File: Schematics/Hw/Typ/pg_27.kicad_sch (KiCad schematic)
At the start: 29 parts, among them U2901 F04, U2902 F04, U2903 F02, U2904 F02, U2905 F02, U2906 F02, U2907 F10, U2908 F138, U2909 F00, U2910 F10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

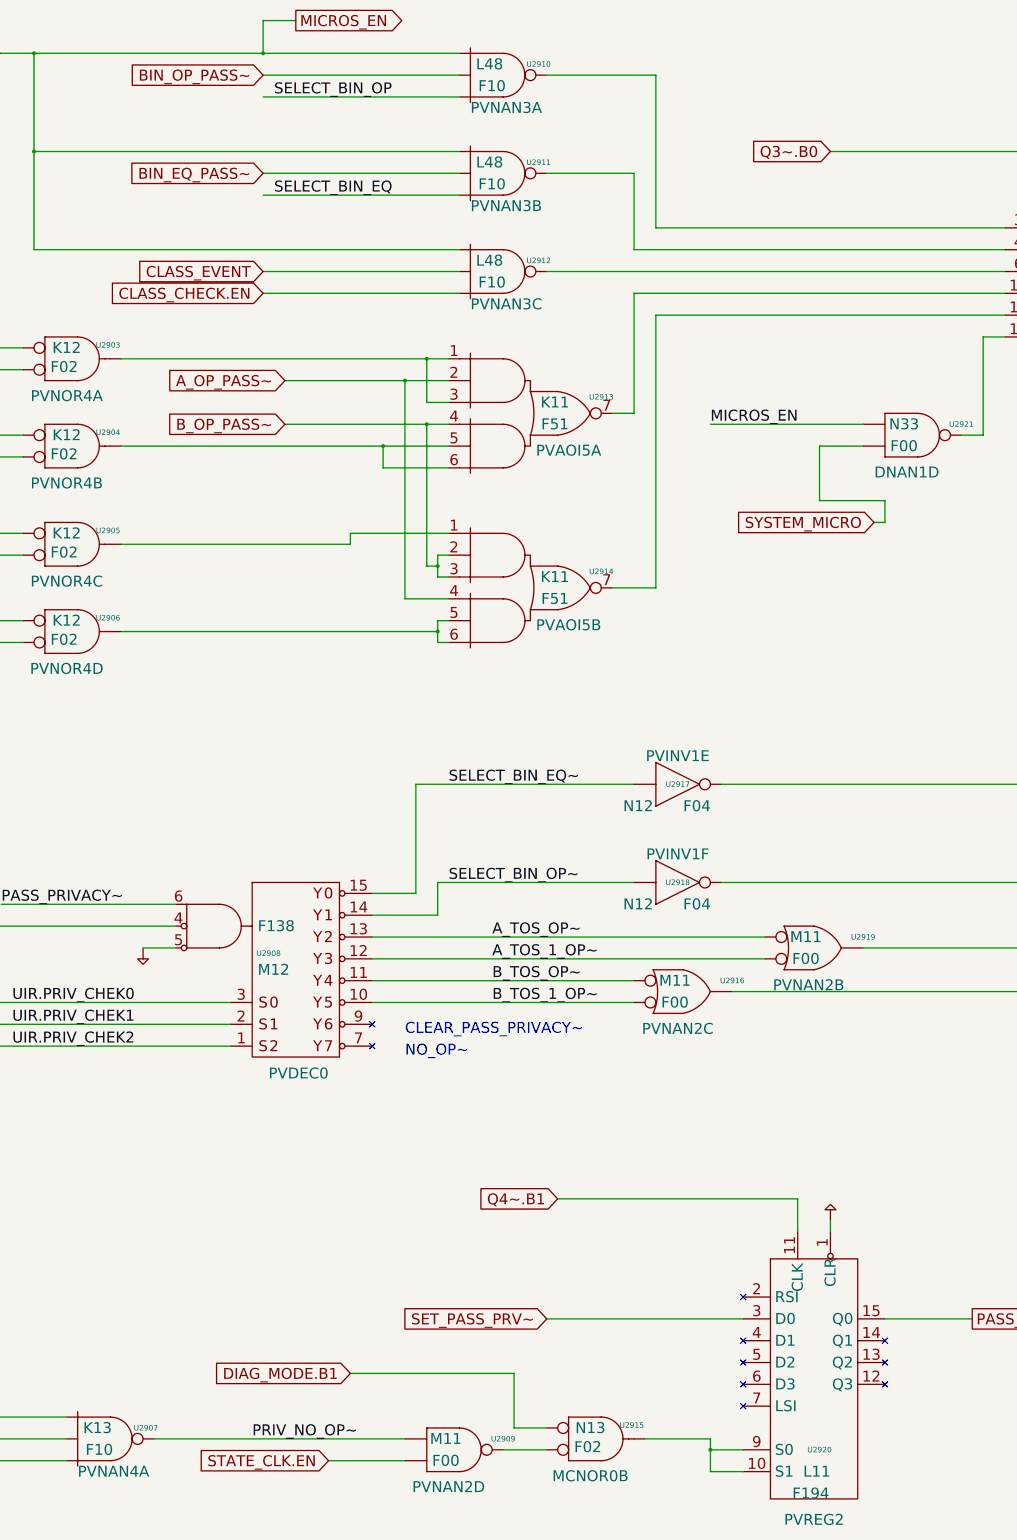
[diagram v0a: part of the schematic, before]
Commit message: Upgrade to KiCad9
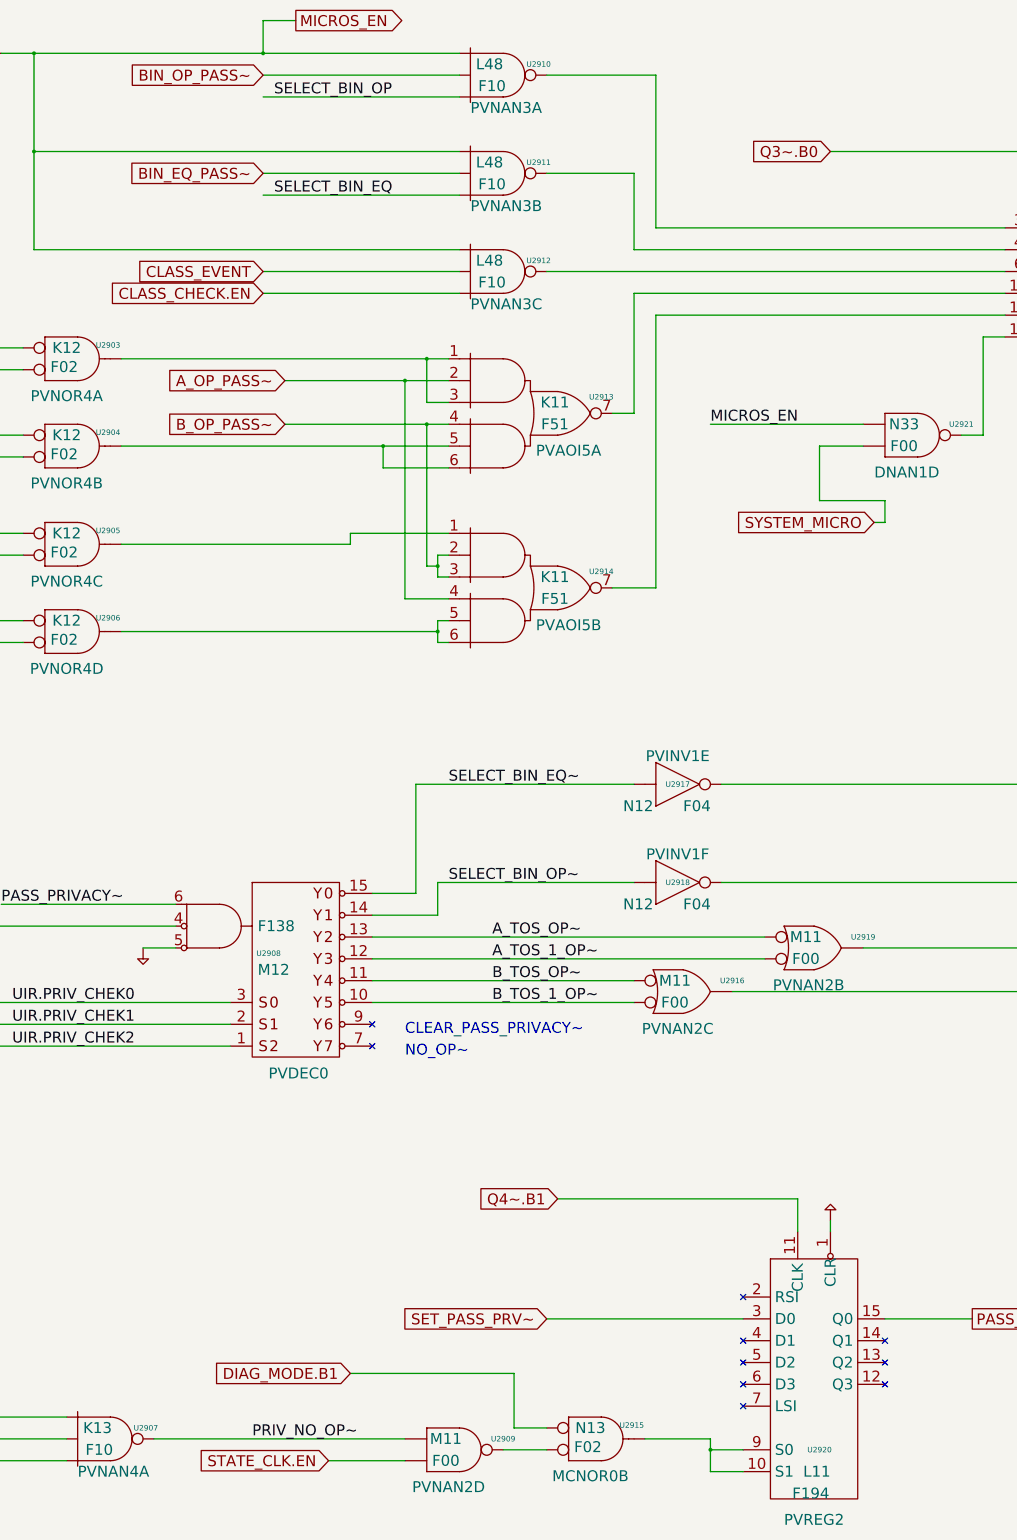
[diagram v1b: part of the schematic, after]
